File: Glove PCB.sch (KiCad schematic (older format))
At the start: 35 parts, among them J1 USB_B_Micro, J2 Conn_01x06_Female, J3 Conn_01x04_Female, J5 Conn_01x06_Female, SW1 TS-1109S-B-B, U3 113990582

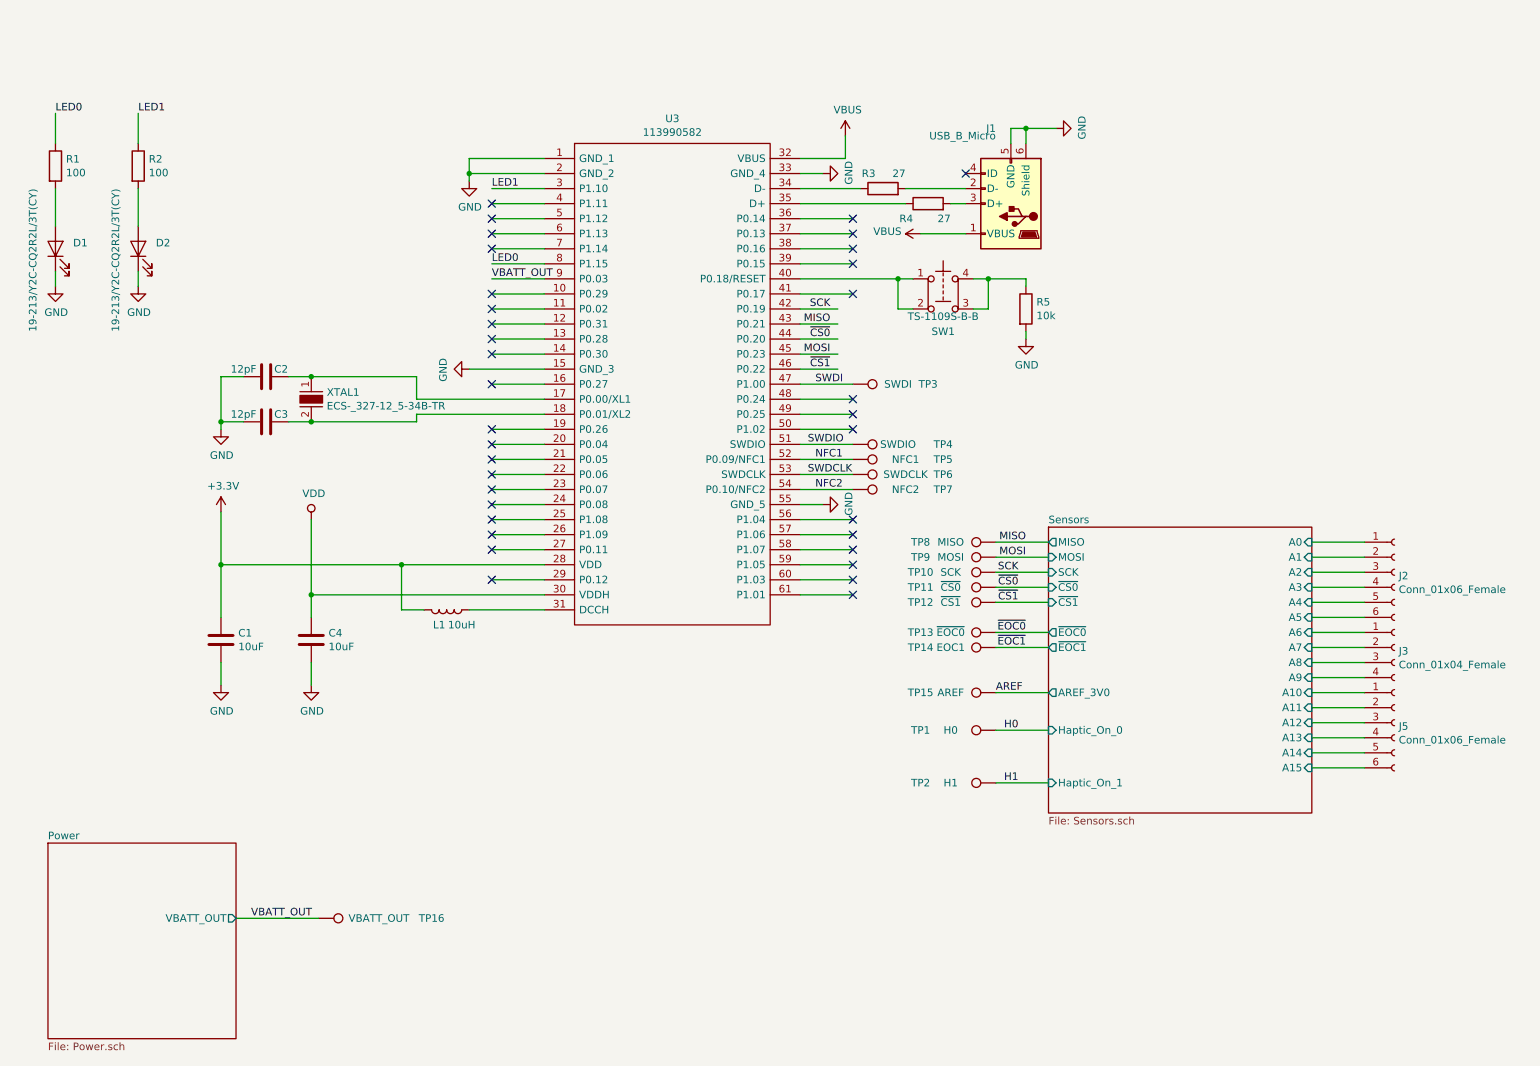
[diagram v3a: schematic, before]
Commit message: Changed to 4-layer board, added power shapes in layout.
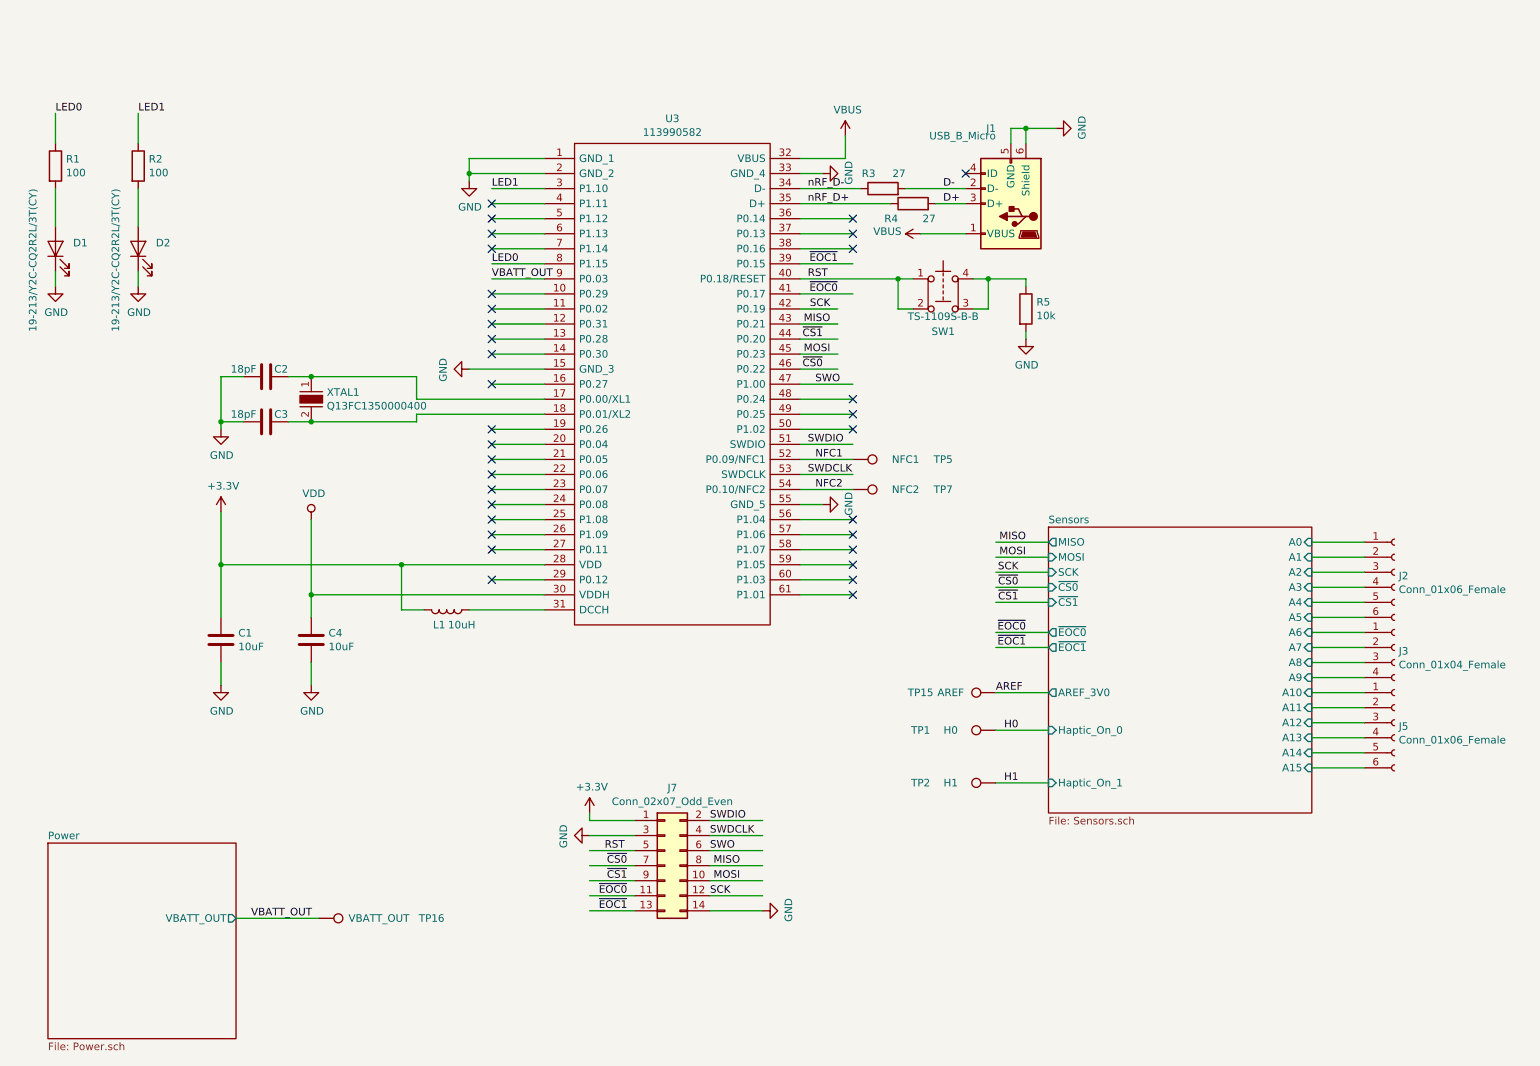
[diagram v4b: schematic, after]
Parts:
- removed TP10: SCK, TestPoint:TestPoint_Pad_D1.5mm, symbol Connector:TestPoint
- removed TP11: ~CS0, TestPoint:TestPoint_Pad_D1.5mm, symbol Connector:TestPoint
- removed TP12: ~CS1, TestPoint:TestPoint_Pad_D1.5mm, symbol Connector:TestPoint
- removed TP13: ~EOC0, TestPoint:TestPoint_Pad_D1.5mm, symbol Connector:TestPoint
- removed TP14: EOC1, TestPoint:TestPoint_Pad_D1.5mm, symbol Connector:TestPoint
- removed TP3: SWDI, TestPoint:TestPoint_Pad_D1.5mm, symbol Connector:TestPoint
- removed TP4: SWDIO, TestPoint:TestPoint_Pad_D1.5mm, symbol Connector:TestPoint
- removed TP6: SWDCLK, TestPoint:TestPoint_Pad_D1.5mm, symbol Connector:TestPoint
- removed TP8: MISO, TestPoint:TestPoint_Pad_D1.5mm, symbol Connector:TestPoint
- removed TP9: MOSI, TestPoint:TestPoint_Pad_D1.5mm, symbol Connector:TestPoint
- added J7: Conn_02x07_Odd_Even, Connector_PinHeader_2.54mm:PinHeader_2x07_P2.54mm_Vertical, symbol Connector_Generic:Conn_02x07_Odd_Even
- C2, C3: value 12pF -> 18pF
- XTAL1: value ECS-_327-12_5-34B-TR -> Q13FC1350000400
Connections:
- net labels added: D+, D-, RST, SWO, nRF_D+, nRF_D-
- net labels removed: SWDI
- wire segments 132 -> 147
- no-connect marks 35 -> 33
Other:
- moved on the sheet: R4
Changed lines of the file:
@@
 P 2750 3150
 F 0 "XTAL1" V 2704 3253 50  0000 L CNN
-F 1 "ECS-_327-12_5-34B-TR" V 2795 3253 50  0000 L CNN
+F 1 "Q13FC1350000400" V 2795 3253 50  0000 L CNN
 F 2 "SamacSys_Parts:ECX-31B" H 2950 3350 60  0001 L CNN
-F 3 "http://www.ecsxtal.com/store/pdf/ecx-31b.pdf" H 2950 3450 60  0001 L CNN
+F 3 "https://datasheet.lcsc.com/szlcsc/1901081604_Seiko-Epson-Q13FC1350000400_C32346.pdf" H 2950 3450 60  0001 L CNN
 F 4 "XC1617CT-ND" H 2950 3550 60  0001 L CNN "Digi-Key_PN"
 F 5 "ECS-.327-12.5-34B-TR" H 2950 3650 60  0001 L CNN "MPN"
@@
 P 2450 3000
 F 0 "C2" V 2400 3100 50  0000 C CNN
-F 1 "12pF" V 2400 2850 50  0000 C CNN
+F 1 "18pF" V 2400 2850 50  0000 C CNN
 F 2 "Capacitor_SMD:C_0402_1005Metric" H 2488 2850 50  0001 C CNN
 F 3 "https://www.digikey.com/en/products/detail/murata-electronics/GCQ1555C1HR12WB01D/7803236" H 2450 3000 50  0001 C CNN
@@
 P 2450 3300
 F 0 "C3" V 2400 3400 50  0000 C CNN
-F 1 "12pF" V 2400 3150 50  0000 C CNN
+F 1 "18pF" V 2400 3150 50  0000 C CNN
 F 2 "Capacitor_SMD:C_0402_1005Metric" H 2488 3150 50  0001 C CNN
 F 3 "https://www.digikey.com/en/products/detail/murata-electronics/GCQ1555C1HR12WB01D/7803236" H 2450 3300 50  0001 C CNN
@@
 L Device:R R4
 U 1 1 5FB6DB5D
-P 6850 1850
-F 0 "R4" V 6750 1950 50  0000 L CNN
-F 1 "27" V 6750 1700 50  0000 L CNN
-F 2 "Resistor_SMD:R_0603_1608Metric_Pad0.84x1.00mm_HandSolder" V 6780 1850 50  0001 C CNN
-F 3 "https://www.digikey.com/en/products/detail/yageo/RT0603FRE0727RL/1075255" H 6850 1850 50  0001 C CNN
-	1    6850 1850
+P 6750 1850
+F 0 "R4" V 6650 1950 50  0000 L CNN
+F 1 "27" V 6650 1700 50  0000 L CNN
+F 2 "Resistor_SMD:R_0603_1608Metric_Pad0.84x1.00mm_HandSolder" V 6680 1850 50  0001 C CNN
+F 3 "https://www.digikey.com/en/products/detail/yageo/RT0603FRE0727RL/1075255" H 6750 1850 50  0001 C CNN
+	1    6750 1850
 	0    -1   -1   0
 $EndComp
@@
 	6700 1750 7100 1750
 Wire Wire Line
-	7000 1850 7100 1850
+	6900 1850 7100 1850
 $Comp
 L Device:R R5
@@
 Text Label 6200 2650 2    50   ~ 0
 MISO
-Text Label 6200 2750 2    50   ~ 0
+Text Label 6150 2950 2    50   ~ 0
 ~CS0
 Text Label 6200 2850 2    50   ~ 0
 MOSI
-Text Label 6200 2950 2    50   ~ 0
+Text Label 6150 2750 2    50   ~ 0
 ~CS1
 Connection ~ 3800 1650
@@
 	6000 1750 6400 1750
 Wire Wire Line
-	6000 1850 6700 1850
+	6000 1850 6600 1850
 Wire Wire Line
 	6000 1550 6300 1550
@@
 	0    -1   -1   0
 $EndComp
-$Comp
-L power:+3.3V #PWR04
-U 1 1 5FE9A7A9
-P 2150 3900
-F 0 "#PWR04" H 2150 3750 50  0001 C CNN
-F 1 "+3.3V" H 2165 4073 50  0000 C CNN
-F 2 "" H 2150 3900 50  0001 C CNN
-F 3 "" H 2150 3900 50  0001 C CNN
-	1    2150 3900
-	1    0    0    -1
-$EndComp
 Wire Wire Line
 	2150 3900 2150 4250
@@
 Wire Wire Line
 	9750 5500 9400 5500
-Wire Wire Line
-	9750 5600 9400 5600
 Wire Wire Line
 	6000 2550 6250 2550
@@
 LED1
 $Comp
-L Connector:TestPoint TP8
-U 1 1 5FFF8A11
-P 7300 4100
-F 0 "TP8" V 7300 4600 50  0000 C CNN
-F 1 "MISO" V 7300 4400 50  0000 C CNN
-F 2 "TestPoint:TestPoint_Pad_D1.5mm" H 7500 4100 50  0001 C CNN
-F 3 "~" H 7500 4100 50  0001 C CNN
-	1    7300 4100
-	0    -1   -1   0
-$EndComp
-$Comp
-L Connector:TestPoint TP9
-U 1 1 5FFF9BD0
-P 7300 4200
-F 0 "TP9" V 7300 4700 50  0000 C CNN
-F 1 "MOSI" V 7300 4500 50  0000 C CNN
-F 2 "TestPoint:TestPoint_Pad_D1.5mm" H 7500 4200 50  0001 C CNN
-F 3 "~" H 7500 4200 50  0001 C CNN
-	1    7300 4200
-	0    -1   -1   0
-$EndComp
-$Comp
-L Connector:TestPoint TP10
-U 1 1 5FFF9D7F
-P 7300 4300
-F 0 "TP10" V 7300 4800 50  0000 C CNN
-F 1 "SCK" V 7300 4600 50  0000 C CNN
-F 2 "TestPoint:TestPoint_Pad_D1.5mm" H 7500 4300 50  0001 C CNN
-F 3 "~" H 7500 4300 50  0001 C CNN
-	1    7300 4300
-	0    -1   -1   0
-$EndComp
-$Comp
-L Connector:TestPoint TP11
-U 1 1 5FFF9FCD
-P 7300 4400
-F 0 "TP11" V 7300 4900 50  0000 C CNN
-F 1 "~CS0" V 7300 4700 50  0000 C CNN
-F 2 "TestPoint:TestPoint_Pad_D1.5mm" H 7500 4400 50  0001 C CNN
-F 3 "~" H 7500 4400 50  0001 C CNN
-	1    7300 4400
-	0    -1   -1   0
-$EndComp
-$Comp
-L Connector:TestPoint TP12
-U 1 1 5FFFA131
-P 7300 4500
-F 0 "TP12" V 7300 5000 50  0000 C CNN
-F 1 "~CS1" V 7300 4800 50  0000 C CNN
-F 2 "TestPoint:TestPoint_Pad_D1.5mm" H 7500 4500 50  0001 C CNN
-F 3 "~" H 7500 4500 50  0001 C CNN
-	1    7300 4500
-	0    -1   -1   0
-$EndComp
-$Comp
-L Connector:TestPoint TP13
-U 1 1 5FFFA2FA
-P 7300 4700
-F 0 "TP13" V 7300 5200 50  0000 C CNN
-F 1 "~EOC0" V 7300 5000 50  0000 C CNN
-F 2 "TestPoint:TestPoint_Pad_D1.5mm" H 7500 4700 50  0001 C CNN
-F 3 "~" H 7500 4700 50  0001 C CNN
-	1    7300 4700
-	0    -1   -1   0
-$EndComp
-$Comp
-L Connector:TestPoint TP14
-U 1 1 5FFFA594
-P 7300 4800
-F 0 "TP14" V 7300 5300 50  0000 C CNN
-F 1 "EOC1" V 7300 5100 50  0000 C CNN
-F 2 "TestPoint:TestPoint_Pad_D1.5mm" H 7500 4800 50  0001 C CNN
-F 3 "~" H 7500 4800 50  0001 C CNN
-	1    7300 4800
-	0    -1   -1   0
-$EndComp
-$Comp
 L Connector:TestPoint TP1
 U 1 1 5FFFA7D4
@@
 	1    7300 5700
 	0    -1   -1   0
-$EndComp
-$Comp
-L Connector:TestPoint TP3
-U 1 1 6000AAB2
-P 6350 3050
-F 0 "TP3" V 6350 3550 50  0000 C CNN
-F 1 "SWDI" V 6350 3350 50  0000 C CNN
-F 2 "TestPoint:TestPoint_Pad_D1.5mm" H 6550 3050 50  0001 C CNN
-F 3 "~" H 6550 3050 50  0001 C CNN
-	1    6350 3050
-	0    1    1    0
-$EndComp
-$Comp
-L Connector:TestPoint TP6
-U 1 1 6000B7CE
-P 6350 3650
-F 0 "TP6" V 6350 4250 50  0000 C CNN
-F 1 "SWDCLK" V 6350 4000 50  0000 C CNN
-F 2 "TestPoint:TestPoint_Pad_D1.5mm" H 6550 3650 50  0001 C CNN
-F 3 "~" H 6550 3650 50  0001 C CNN
-	1    6350 3650
-	0    1    1    0
 $EndComp
 $Comp
@@
 NoConn ~ 6350 2050
 NoConn ~ 6350 2150
-NoConn ~ 6350 2250
-NoConn ~ 6350 2450
 NoConn ~ 6350 3150
 NoConn ~ 6350 3250
@@
 SWDIO
 Text Label 6100 3050 0    50   ~ 0
-SWDI
+SWO
 Text Label 6100 3550 0    50   ~ 0
 NFC1
@@
 	0    1    1    0
 $EndComp
-$Comp
-L Connector:TestPoint TP4
-U 1 1 6000C0EB
-P 6350 3450
-F 0 "TP4" V 6350 4050 50  0000 C CNN
-F 1 "SWDIO" V 6350 3750 50  0000 C CNN
-F 2 "TestPoint:TestPoint_Pad_D1.5mm" H 6550 3450 50  0001 C CNN
-F 3 "~" H 6550 3450 50  0001 C CNN
-	1    6350 3450
-	0    1    1    0
-$EndComp
 Wire Wire Line
 	6750 2550 6650 2550
@@
 Text Label 3950 1750 0    50   ~ 0
 LED1
+Wire Wire Line
+	9400 5600 9750 5600
+Text Label 6050 2350 0    50   ~ 0
+RST
+$Comp
+L Connector_Generic:Conn_02x07_Odd_Even J7
+U 1 1 5FCD1648
+P 5100 6250
+F 0 "J7" H 5150 6767 50  0000 C CNN
+F 1 "Conn_02x07_Odd_Even" H 5150 6676 50  0000 C CNN
+F 2 "Connector_PinHeader_2.54mm:PinHeader_2x07_P2.54mm_Vertical" H 5100 6250 50  0001 C CNN
+F 3 "~" H 5100 6250 50  0001 C CNN
+	1    5100 6250
+	1    0    0    -1
+$EndComp
+Wire Wire Line
+	4900 5950 4600 5950
+Wire Wire Line
+	4600 6550 4900 6550
+Wire Wire Line
+	4900 6450 4600 6450
+Wire Wire Line
+	4900 6350 4600 6350
+Wire Wire Line
+	4900 6250 4600 6250
+Wire Wire Line
+	4900 6150 4600 6150
+Wire Wire Line
+	4900 6050 4600 6050
+Wire Wire Line
+	5400 5950 5750 5950
+Wire Wire Line
+	5750 6550 5400 6550
+Wire Wire Line
+	5400 6450 5750 6450
+Wire Wire Line
+	5400 6350 5750 6350
+Wire Wire Line
+	5400 6250 5750 6250
+Wire Wire Line
+	5400 6150 5750 6150
+Wire Wire Line
+	5400 6050 5750 6050
+$Comp
+L power:GND #PWR0103
+U 1 1 5FD36CBB
+P 4600 6050
+F 0 "#PWR0103" H 4600 5800 50  0001 C CNN
+F 1 "GND" H 4605 5877 50  0000 C CNN
+F 2 "" H 4600 6050 50  0001 C CNN
+F 3 "" H 4600 6050 50  0001 C CNN
+	1    4600 6050
+	0    1    1    0
+$EndComp
+$Comp
+L power:+3.3V #PWR04
+U 1 1 5FE9A7A9
+P 2150 3900
+F 0 "#PWR04" H 2150 3750 50  0001 C CNN
+F 1 "+3.3V" H 2165 4073 50  0000 C CNN
+F 2 "" H 2150 3900 50  0001 C CNN
+F 3 "" H 2150 3900 50  0001 C CNN
+	1    2150 3900
+	1    0    0    -1
+$EndComp
+$Comp
+L power:+3.3V #PWR0104
+U 1 1 5FD3FA8F
+P 4600 5900
+F 0 "#PWR0104" H 4600 5750 50  0001 C CNN
+F 1 "+3.3V" H 4615 6073 50  0000 C CNN
+F 2 "" H 4600 5900 50  0001 C CNN
+F 3 "" H 4600 5900 50  0001 C CNN
+	1    4600 5900
+	1    0    0    -1
+$EndComp
+Wire Wire Line
+	4600 5950 4600 5900
+Text Label 5400 5950 0    50   ~ 0
+SWDIO
+Text Label 5400 6050 0    50   ~ 0
+SWDCLK
+Text Label 5400 6150 0    50   ~ 0
+SWO
+Text Label 4700 6150 0    50   ~ 0
+RST
+Text Label 4850 6250 2    50   ~ 0
+~CS0
+Text Label 4850 6350 2    50   ~ 0
+~CS1
+Text Label 4850 6450 2    50   ~ 0
+~EOC0
+Text Label 4850 6550 2    50   ~ 0
+~EOC1
+Text Label 5600 6250 2    50   ~ 0
+MISO
+Text Label 5600 6350 2    50   ~ 0
+MOSI
+Text Label 5400 6450 0    50   ~ 0
+SCK
+$Comp
+L power:GND #PWR0105
+U 1 1 5FD49AE3
+P 5750 6550
+F 0 "#PWR0105" H 5750 6300 50  0001 C CNN
+F 1 "GND" H 5755 6377 50  0000 C CNN
+F 2 "" H 5750 6550 50  0001 C CNN
+F 3 "" H 5750 6550 50  0001 C CNN
+	1    5750 6550
+	0    -1   -1   0
+$EndComp
+Text Label 6250 2450 2    50   ~ 0
+~EOC0
+Text Label 6250 2250 2    50   ~ 0
+~EOC1
+Text Label 6950 1850 0    50   ~ 0
+D+
+Text Label 6950 1750 0    50   ~ 0
+D-
+Text Label 6050 1750 0    50   ~ 0
+nRF_D-
+Text Label 6050 1850 0    50   ~ 0
+nRF_D+
 $EndSCHEMATC
